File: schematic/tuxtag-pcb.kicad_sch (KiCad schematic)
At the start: 10 parts, among them J1 vibrator, J2 battery, J3 buzzer, Q1 P2N2222A, U1 ESP32-C3_SUPERMINI_TH

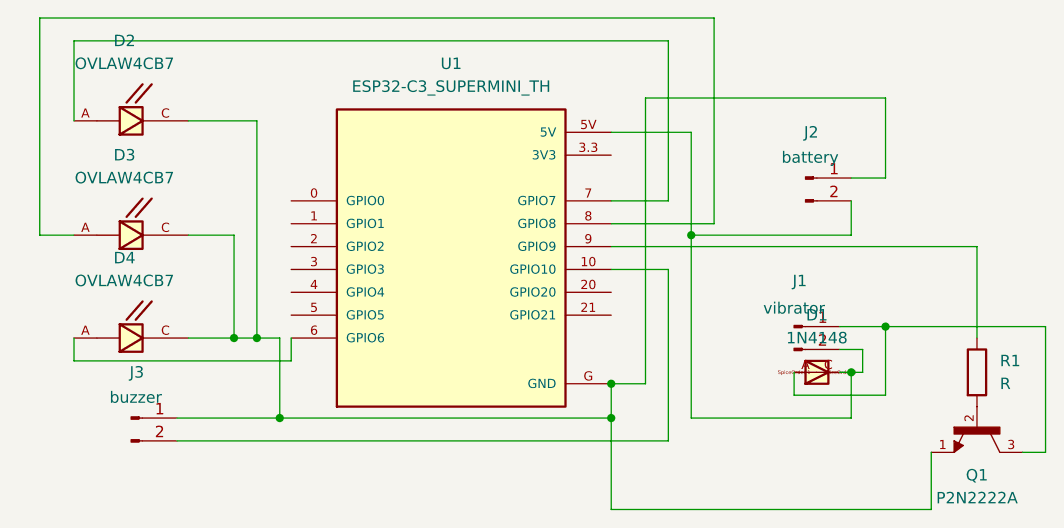
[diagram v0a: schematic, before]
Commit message: Added resistors to LEDs
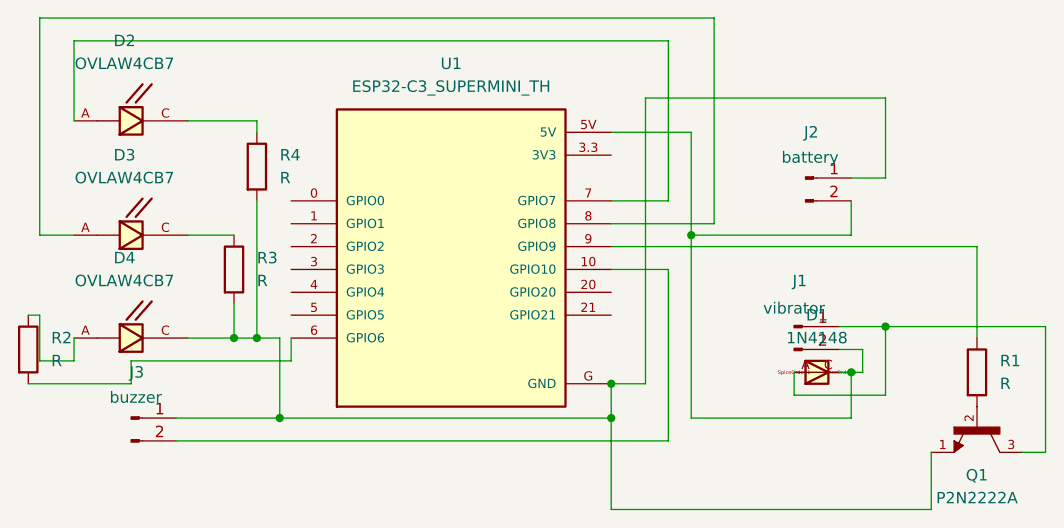
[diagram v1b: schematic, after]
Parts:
- added R2, R3, R4: R, Resistor_THT:R_Axial_DIN0204_L3.6mm_D1.6mm_P5.08mm_Horizontal, symbol Device:R
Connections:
- net at D4.A: now also R2.1; no longer U1.6 (GPIO6)
- net at D4.C, J2.1 (Pin_1), J3.1 (Pin_1)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: now also R3.2, R4.2; no longer D2.C, D3.C
- new net: D2.C, R4.1
- new net: R2.2, U1.6 (GPIO6)
- new net: D3.C, R3.1
